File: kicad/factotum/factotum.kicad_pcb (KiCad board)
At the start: 2 copper layers, 90 x 100 mm, 146 parts, among them J1 Conn_01x06, J10 OUT3, J11 OUT5, J12 OUT7, J13 Conn_01x10_Female, J14 OUT2, J15 OUT4, J16 OUT6, J17 OUT8, J18 Conn_01x10_Male, J19 Conn_01x18_Female, J2 USART, J20 Conn_01x18_Male, J3 Conn_02x05_Odd_Even, J4 Conn_01x10_Female, J5 VOCT, J6 Conn_01x10_Male, J7 SCL, J8 CLK, J9 OUT1, P1 10k, P2 10k, P3 10k, P4 10k, SW1 MODE_SW, U1 STM32F411RETx, U10 DAC128S085, U15 PCA9685PW, U2 R-78E3.3-0.5, U3 LD2981ABU33, U4 MCP6004, U5 ADC128S022, U6 LM2902, U7 LM2902, Y1 16 MHz

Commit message: small move
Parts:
- moved D10 0.63 mm to (125.7, 41.3)
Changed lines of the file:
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@@
   )
   (module LED_THT:LED_D3.0mm-3 (layer F.Cu)
-    (at 125.73 40.64 180)
+    (at 125.73 41.275 180)
     (descr "LED, diameter 3.0mm, 2 pins, diameter 3.0mm, 3 pins, http://www.kingbright.com/attachments/file/psearch/000/00/00/L-3VSURKCGKC(Ver.8A).pdf")
     (tags "LED diameter 3.0mm 2 pins diameter 3.0mm 3 pins")

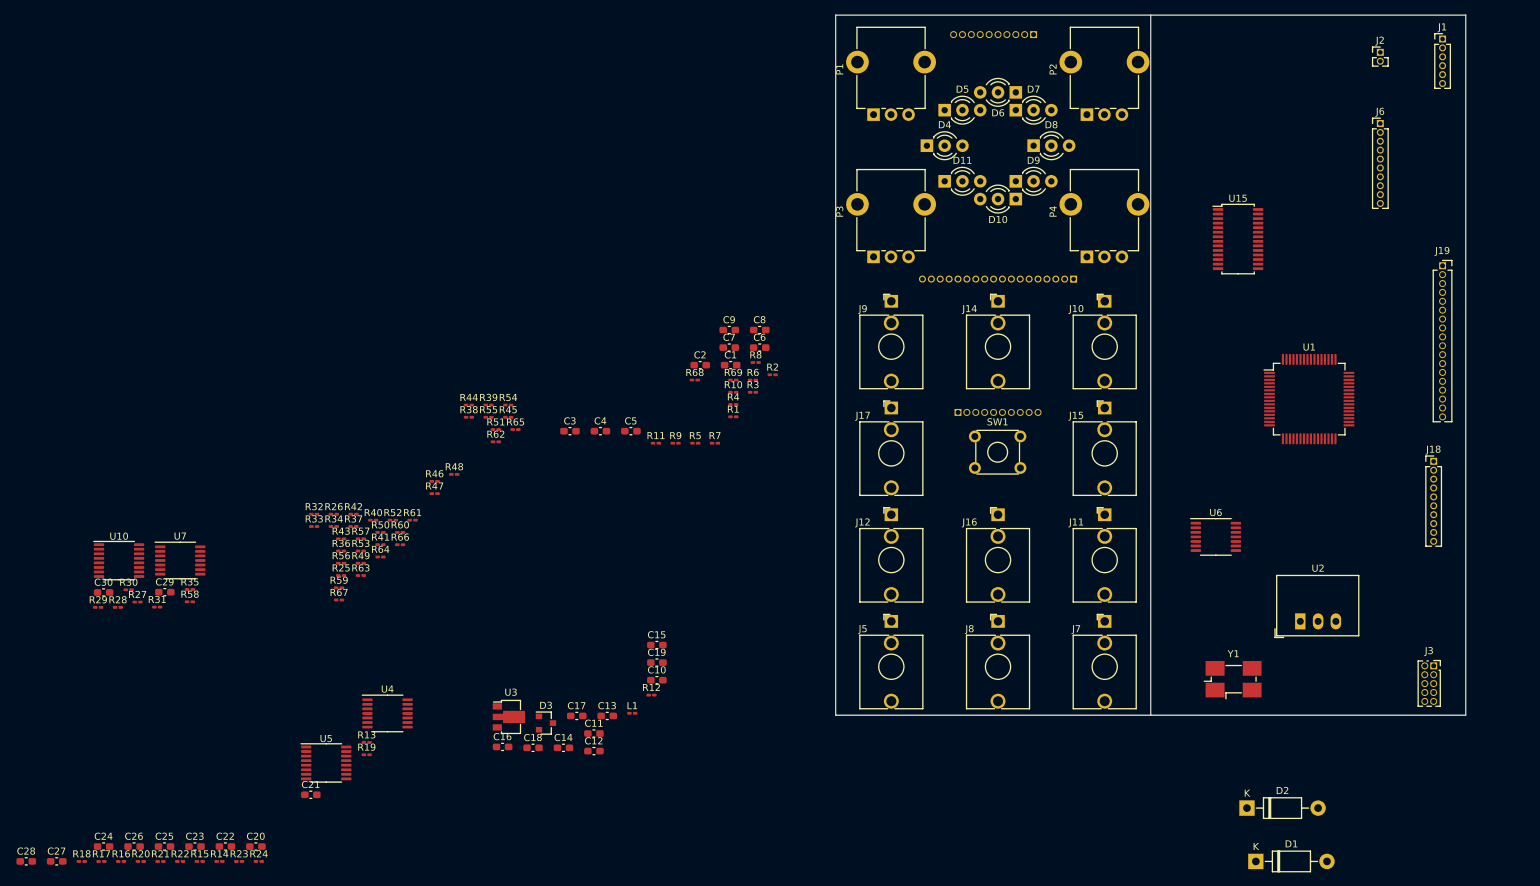
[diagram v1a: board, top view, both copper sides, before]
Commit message: inital board layout done but not routed
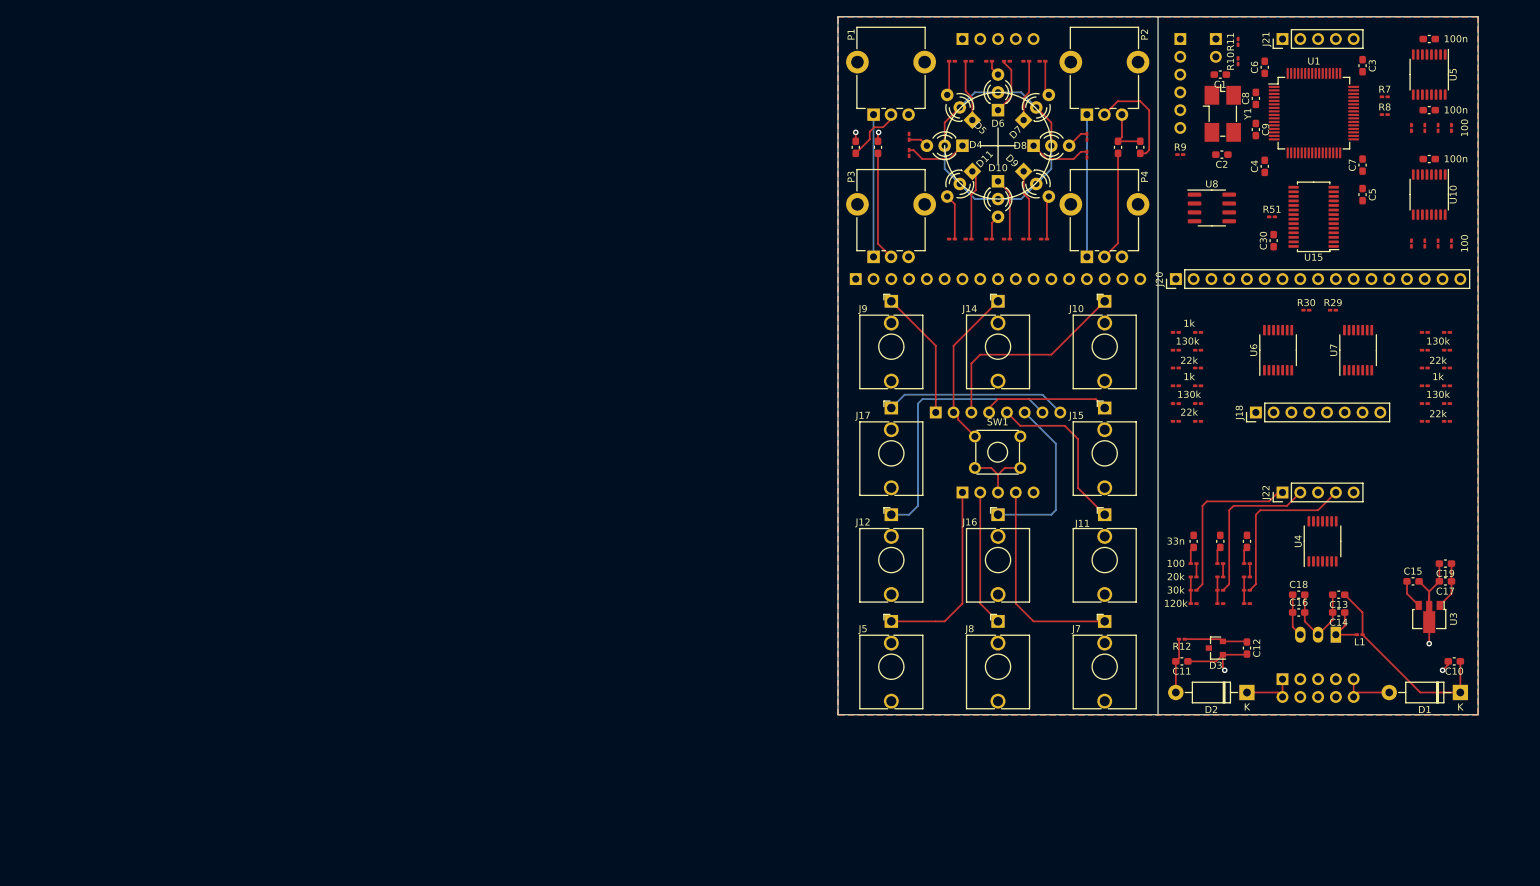
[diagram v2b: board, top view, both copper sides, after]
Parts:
- added J21: Conn_01x05_Male, Connector_PinHeader_2.54mm:PinHeader_1x05_P2.54mm_Vertical, F.Cu at (163.8, 18.4)
- added J22: Conn_01x05_Male, Connector_PinHeader_2.54mm:PinHeader_1x05_P2.54mm_Vertical, F.Cu at (163.8, 83.2)
- added U8: M24C02-RMN, Package_SO:SOIC-8_3.9x4.9mm_P1.27mm, F.Cu at (153.7, 42.5)
- J1: footprint Connector_PinHeader_1.27mm:PinHeader_1x06_P1.27mm_Vertical -> Connector_PinHeader_2.54mm:PinHeader_1x06_P2.54mm_Vertical; moved to B.Cu
- J13: value Conn_01x10_Female -> Conn_01x08_Female; footprint Connector_PinSocket_1.27mm:PinSocket_1x10_P1.27mm_Vertical -> Connector_PinSocket_2.54mm:PinSocket_1x08_P2.54mm_Vertical
- J18: value Conn_01x10_Male -> Conn_01x08_Male; footprint Connector_PinHeader_1.27mm:PinHeader_1x10_P1.27mm_Vertical -> Connector_PinHeader_2.54mm:PinHeader_1x08_P2.54mm_Vertical
- J19: value Conn_01x18_Female -> Conn_01x17_Female; footprint Connector_PinSocket_1.27mm:PinSocket_1x18_P1.27mm_Vertical -> Connector_PinSocket_2.54mm:PinSocket_1x17_P2.54mm_Vertical; moved to B.Cu
- J2: footprint Connector_PinHeader_1.27mm:PinHeader_1x02_P1.27mm_Vertical -> Connector_PinHeader_2.54mm:PinHeader_1x02_P2.54mm_Vertical; moved to B.Cu
- J20: value Conn_01x18_Male -> Conn_01x17_Male; footprint Connector_PinHeader_1.27mm:PinHeader_1x18_P1.27mm_Vertical -> Connector_PinHeader_2.54mm:PinHeader_1x17_P2.54mm_Vertical; moved to F.Cu
- J3: footprint Connector_PinSocket_1.27mm:PinSocket_2x05_P1.27mm_Vertical -> Connector_PinHeader_2.54mm:PinHeader_2x05_P2.54mm_Vertical; moved to B.Cu
- J4: value Conn_01x10_Female -> Conn_01x05_Female; footprint Connector_PinSocket_1.27mm:PinSocket_1x10_P1.27mm_Vertical -> Connector_PinSocket_2.54mm:PinSocket_1x05_P2.54mm_Vertical
- J6: value Conn_01x10_Male -> Conn_01x05_Female; footprint Connector_PinHeader_1.27mm:PinHeader_1x10_P1.27mm_Vertical -> Connector_PinSocket_2.54mm:PinSocket_1x05_P2.54mm_Vertical; moved to B.Cu
- U2: moved to B.Cu
- moved C27 223.5 mm to (184.8, 28.6), turned to 180 degrees
- moved C25 205.6 mm to (184.8, 35.6), turned to 180 degrees
- moved C29 197.1 mm to (184.8, 18.4), turned to 180 degrees
- moved U10 194.3 mm to (184.8, 40.6), turned to 270 degrees
- moved U5 185.7 mm to (184.8, 23.5), turned to 270 degrees
- moved R29 181.4 mm to (171.0, 57.1)
- moved C28 180.3 mm to (158.8, 90.2), turned to 90 degrees
- moved C30 174.5 mm to (162.6, 47.2), turned to 90 degrees
- moved R30 172.9 mm to (167.2, 57.1)
- moved C26 172.4 mm to (140.3, 33.9), turned to 90 degrees
- moved U7 170.9 mm to (174.6, 62.9), turned to 90 degrees
- moved R18 167.2 mm to (154.9, 97.2)
- moved C24 165.4 mm to (154.9, 90.2), turned to 90 degrees
- moved C22 164.5 mm to (143.5, 33.9), turned to 90 degrees
- moved R17 164.0 mm to (154.9, 99.1)
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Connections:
- net ADC_VC_SCL renamed ADC_RST
- C23 pad 1: T_SCL -> T_OFF
- C26 pad 1: T_OFF -> T_SCL
- J13 pad 1: VREF -> T_1
- J13 pad 2: T_1 -> T_2
- J13 pad 3: T_2 -> T_3
- J13 pad 4: T_3 -> T_4
- J13 pad 5: T_4 -> T_5
- J13 pad 6: T_5 -> T_6
- J13 pad 7: T_6 -> T_7
- J13 pad 8: T_7 -> T_8
- J18 pad 1: VREF -> B_1
- J18 pad 2: B_1 -> B_2
- J18 pad 3: B_2 -> B_3
- J18 pad 4: B_3 -> B_4
- J18 pad 5: B_4 -> B_5
- J18 pad 6: B_5 -> B_6
- J18 pad 7: B_6 -> B_7
- J18 pad 8: B_7 -> B_8
- J19 pad 1: +3V3 -> G8_T
- J19 pad 10: Net-(J19-Pad10) -> R4_T
- J19 pad 11: Net-(J19-Pad11) -> G3_T
- J19 pad 12: Net-(J19-Pad12) -> R3_T
- J19 pad 13: Net-(J19-Pad13) -> G2_T
- J19 pad 14: Net-(J19-Pad14) -> R2_T
- J19 pad 15: Net-(J19-Pad15) -> G1_T
- J19 pad 16: Net-(J19-Pad16) -> R1_T
- J19 pad 17: Net-(J19-Pad17) -> +3V3
- J19 pad 2: Net-(J19-Pad2) -> R8_T
- J19 pad 3: Net-(J19-Pad3) -> G7_T
- J19 pad 4: Net-(J19-Pad4) -> R7_T
- J19 pad 5: Net-(J19-Pad5) -> G6_T
- J19 pad 6: Net-(J19-Pad6) -> R6_T
- J19 pad 7: Net-(J19-Pad7) -> G5_T
- J19 pad 8: Net-(J19-Pad8) -> R5_T
- J19 pad 9: Net-(J19-Pad9) -> G4_T
- J20 pad 1: +3V3 -> Net-(J20-Pad1)
- J20 pad 10: R5_T -> Net-(J20-Pad10)
- J20 pad 11: G5_T -> Net-(J20-Pad11)
- J20 pad 12: R6_T -> Net-(J20-Pad12)
- J20 pad 13: G6_T -> Net-(J20-Pad13)
- J20 pad 14: R7_T -> Net-(J20-Pad14)
- J20 pad 15: G7_T -> Net-(J20-Pad15)
- J20 pad 16: R8_T -> Net-(J20-Pad16)
- J20 pad 17: G8_T -> +3V3
- J20 pad 2: R1_T -> Net-(J20-Pad2)
- J20 pad 3: G1_T -> Net-(J20-Pad3)
- J20 pad 4: R2_T -> Net-(J20-Pad4)
- J20 pad 5: G2_T -> Net-(J20-Pad5)
- J20 pad 6: R3_T -> Net-(J20-Pad6)
- J20 pad 7: G3_T -> Net-(J20-Pad7)
- J20 pad 8: R4_T -> Net-(J20-Pad8)
- J20 pad 9: G4_T -> Net-(J20-Pad9)
- J4 pad 3: T_SEL -> T_OFF
- J4 pad 5: T_OFF -> T_SEL
- J6 pad 1: +3.3VA -> T_VOCT
- J6 pad 2: B_FRQ -> T_CLK
- J6 pad 3: B_SEL -> T_MODE
- J6 pad 4: B_SCL -> T_RST
- J6 pad 5: B_OFF -> GND
- J7 pad S: T_SCALE -> T_RST
- P3 pad 2: T_SCL -> T_OFF
- P4 pad 2: T_OFF -> T_SCL
- R18 pad 2: B_SCALE -> B_RST
- U15 pad 10: Net-(J19-Pad6) -> Net-(J20-Pad12)
- U15 pad 11: Net-(J19-Pad7) -> Net-(J20-Pad11)
- U15 pad 12: Net-(J19-Pad8) -> Net-(J20-Pad10)
- U15 pad 13: Net-(J19-Pad9) -> Net-(J20-Pad9)
- U15 pad 15: Net-(J19-Pad10) -> Net-(J20-Pad8)
- U15 pad 16: Net-(J19-Pad11) -> Net-(J20-Pad7)
- U15 pad 17: Net-(J19-Pad12) -> Net-(J20-Pad6)
- U15 pad 18: Net-(J19-Pad13) -> Net-(J20-Pad5)
- U15 pad 19: Net-(J19-Pad14) -> Net-(J20-Pad4)
- U15 pad 20: Net-(J19-Pad15) -> Net-(J20-Pad3)
- U15 pad 21: Net-(J19-Pad16) -> Net-(J20-Pad2)
- U15 pad 22: Net-(J19-Pad17) -> Net-(J20-Pad1)
- U15 pad 6: Net-(J19-Pad2) -> Net-(J20-Pad16)
- U15 pad 7: Net-(J19-Pad3) -> Net-(J20-Pad15)
- U15 pad 8: Net-(J19-Pad4) -> Net-(J20-Pad14)
- U15 pad 9: Net-(J19-Pad5) -> Net-(J20-Pad13)
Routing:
- net +3V3: track 0.00 -> 57.0 mm
- net GND: track 0.00 -> 55.8 mm, vias 0 -> 5
- net +3.3VA: track 0.00 -> 47.3 mm
- net T_7: track 0.00 -> 37.8 mm
- net +12V: track 0.00 -> 32.7 mm
- net T_3: track 0.00 -> 29.7 mm
- net T_RST: track 0.00 -> 29.6 mm
- net T_VOCT: track 0.00 -> 27.1 mm
- net T_8: track 0.00 -> 26.0 mm
- net B_VOCT: track 0.00 -> 24.6 mm
- net T_6: track 0.00 -> 24.3 mm
- net T_5: track 0.00 -> 24.1 mm
- net B_CLK: track 0.00 -> 23.9 mm
- net B_RST: track 0.00 -> 23.0 mm
- net T_CLK: track 0.00 -> 19.5 mm
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- added copper zone on B.Cu, net GND
- added copper zone on F.Cu, net GND
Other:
- board size 90 x 100 mm -> 91.4 x 99.7 mm

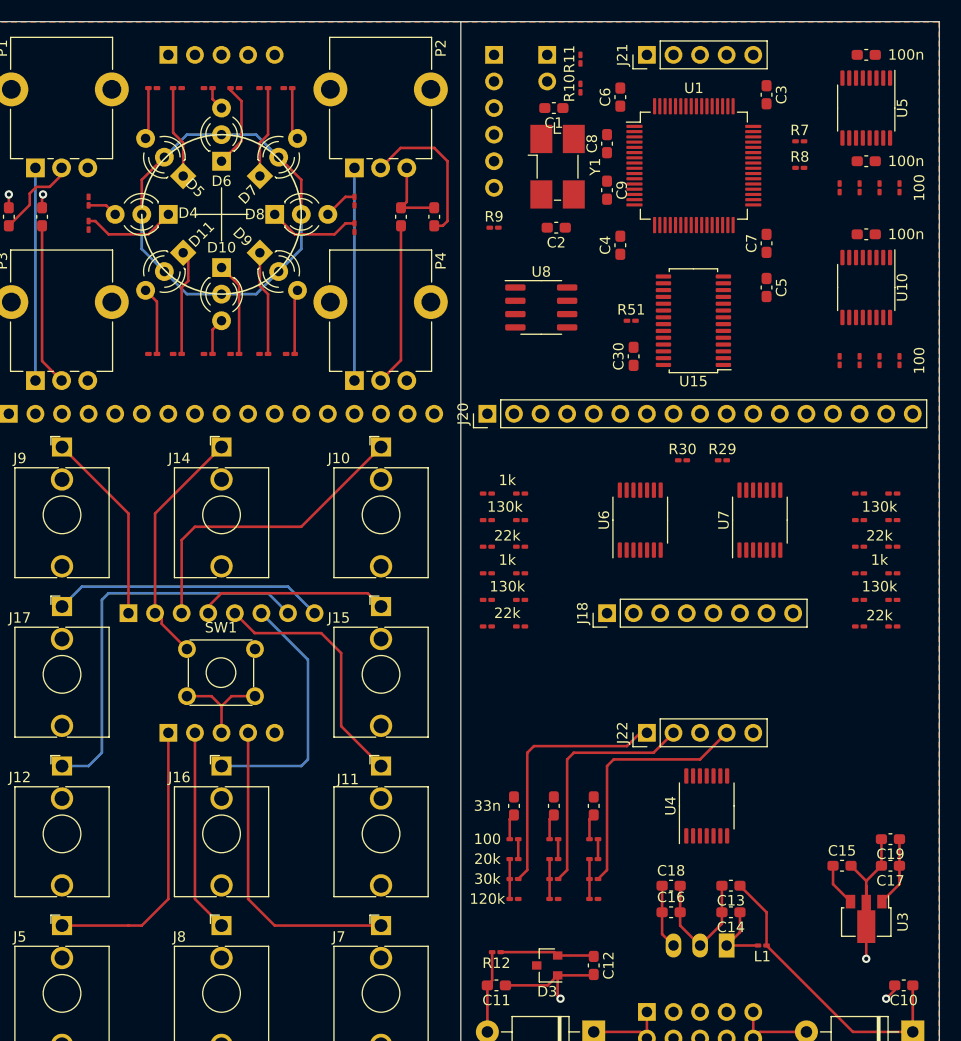
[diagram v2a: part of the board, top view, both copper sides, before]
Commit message: adding switches to inputs; fixing resistor components to 603
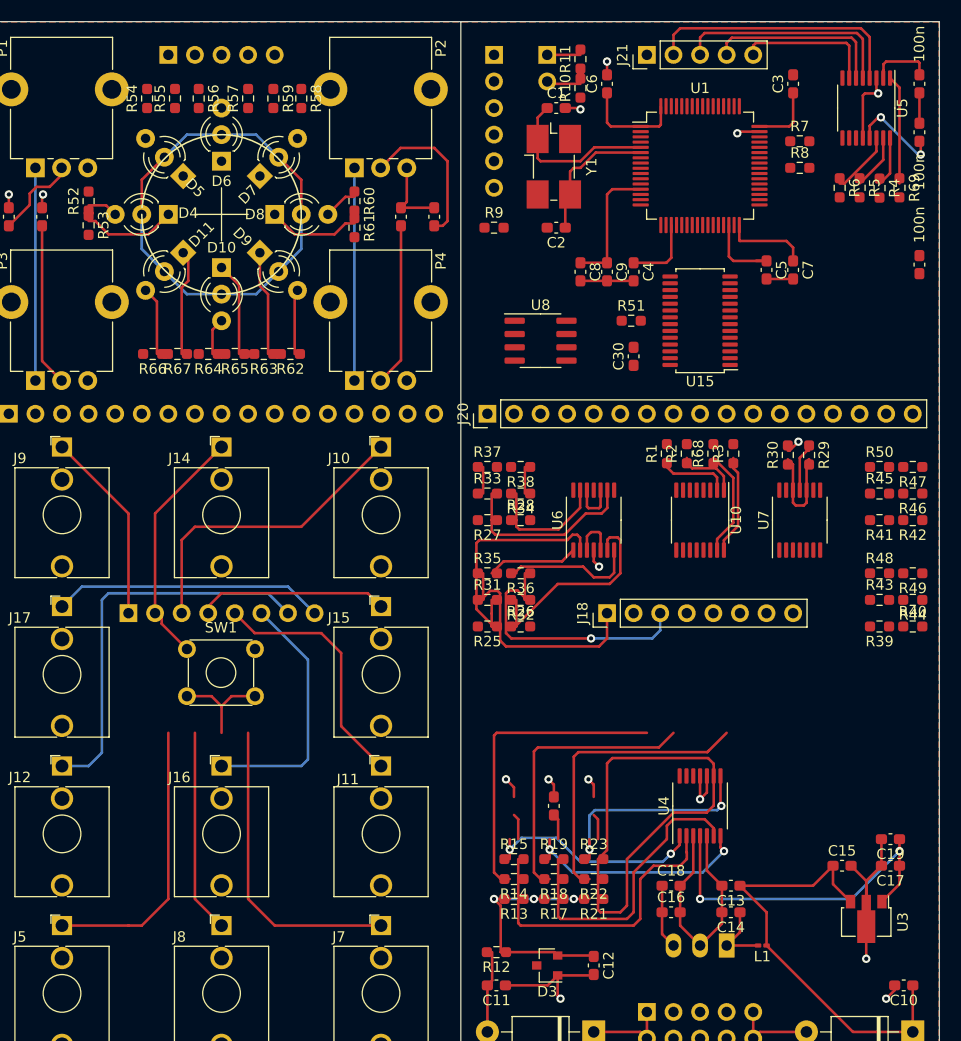
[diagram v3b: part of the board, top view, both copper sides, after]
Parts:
- removed C21, C28: 33n, Capacitor_SMD:C_0603_1608Metric_Pad1.08x0.95mm_HandSolder
- removed J22: Conn_01x05_Male, Connector_PinHeader_2.54mm:PinHeader_1x05_P2.54mm_Vertical
- removed J6: Conn_01x05_Female, Connector_PinSocket_2.54mm:PinSocket_1x05_P2.54mm_Vertical
- removed R16, R20, R24: 100, Resistor_SMD:R_0201_0603Metric_Pad0.64x0.40mm_HandSolder
- C24: value 33n -> 100p
- J7: value SCL -> RST
- R1, R10, R11, R12, R13, R15, R17, R19, R2, R21, R23, R25, R26, R27, R28, R29, R3, R30, R31, R32, R33, R34, R35, R36, R37, R38, R39, R4, R40, R41, R42, R43, R44, R45, R46, R47, R48, R49, R5, R50, R51, R52, R53, R54, R55, R56, R57, R58, R59, R6, R60, R61, R62, R63, R64, R65, R66, R67, R68, R69, R7, R8, R9: footprint Resistor_SMD:R_0201_0603Metric_Pad0.64x0.40mm_HandSolder -> Resistor_SMD:R_0603_1608Metric_Pad0.98x0.95mm_HandSolder
- R14, R18, R22: value 30k -> 120k; footprint Resistor_SMD:R_0201_0603Metric_Pad0.64x0.40mm_HandSolder -> Resistor_SMD:R_0603_1608Metric_Pad0.98x0.95mm_HandSolder
- moved U10 27.3 mm to (168.9, 62.9)
- moved R2 20.4 mm to (167.6, 56.5)
- moved R1 20.4 mm to (165.7, 56.5)
- moved R68 19.9 mm to (170.2, 56.5)
- moved R3 13.5 mm to (172.1, 56.5)
- moved C8 12.5 mm to (157.5, 39.1), turned to 270 degrees
- moved R30 10.1 mm to (177.3, 56.6), turned to 90 degrees
- moved R29 8.30 mm to (179.3, 56.6), turned to 270 degrees
- moved C9 7.80 mm to (160.0, 39.1)
- moved C25 5.85 mm to (189.9, 38.5), turned to 270 degrees
- moved C29 5.78 mm to (189.9, 21.2), turned to 270 degrees
- moved C27 5.78 mm to (189.9, 25.8), turned to 90 degrees
- moved U6 4.44 mm to (158.8, 62.9)
- moved R4 3.81 mm to (186.1, 31.1)
- moved R6 3.81 mm to (182.2, 31.1), turned to 270 degrees
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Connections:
- net Net-(U1-Pad14) renamed B_MODE_SW
- net Net-(U1-Pad15) renamed B_VOCT_SW
- net Net-(U1-Pad16) renamed B_CLK_SW
- net Net-(U1-Pad17) renamed B_RST_SW
- net T_MODE renamed T_MODE_SW
- C24 pad 1: ADC_RST -> Net-(C24-Pad1)
- C24 pad 2: GND -> ADC_VOCT
- J5 pad S: T_VOCT -> GND
- J5 pad T: GND -> T_VOCT
- J5 pad TN: GND -> T_VOCT_SW
- J7 pad S: T_RST -> GND
- J7 pad T: GND -> T_RST
- J7 pad TN: GND -> T_RST_SW
- J8 pad S: T_CLK -> GND
- J8 pad T: GND -> T_CLK
- J8 pad TN: GND -> T_CLK_SW
- R13 pad 1: Net-(R13-Pad1) -> Net-(C24-Pad1)
- R14 pad 1: Net-(R13-Pad1) -> Net-(C24-Pad1)
- R15 pad 1: Net-(R15-Pad1) -> ADC_VOCT
- R15 pad 2: Net-(R13-Pad1) -> Net-(C24-Pad1)
- R19 pad 1: Net-(R19-Pad1) -> ADC_RST
- R23 pad 1: Net-(R23-Pad1) -> ADC_CLK
- U1 pad 26: B_MODE -> Net-(U1-Pad26)
- U4 pad 1: Net-(R15-Pad1) -> ADC_VOCT
- U4 pad 2: Net-(R13-Pad1) -> Net-(C24-Pad1)
- U4 pad 7: Net-(R19-Pad1) -> ADC_RST
- U4 pad 8: Net-(R23-Pad1) -> ADC_CLK
- U5 pad 5: B_SEL -> B_OFF
- U5 pad 7: B_OFF -> B_SEL
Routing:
- net GND: track 55.8 -> 177.0 mm, vias 5 -> 14
- net +3.3VA: track 47.3 -> 97.1 mm, vias 0 -> 2
- net Net-(C28-Pad1): track 3.81 -> 47.0 mm
- net +3V3: track 57.0 -> 97.4 mm, vias 0 -> 2
- net Net-(C24-Pad1): track 0.00 -> 31.9 mm
- net T_RST: track 29.6 -> 0.00 mm
- net T_VOCT: track 27.1 -> 0.00 mm
- net B_3: track 0.00 -> 25.7 mm, vias 0 -> 1
- net B_FRQ: track 0.00 -> 25.2 mm
- net Net-(C21-Pad1): track 3.81 -> 28.5 mm
- net ADC_VOCT: track 2.48 -> 25.5 mm, vias 0 -> 3
- net Net-(R25-Pad1): track 0.00 -> 22.6 mm
- net B_1: track 0.00 -> 22.4 mm
- net B_OFF: track 0.00 -> 21.4 mm
- net ADC_CLK: track 2.48 -> 23.4 mm, vias 0 -> 2
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
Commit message: layout components again
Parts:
- added C21: 100p, Capacitor_SMD:C_0603_1608Metric_Pad1.08x0.95mm_HandSolder, F.Cu at (154.5, 84.5)
- added C28: 100p, Capacitor_SMD:C_0603_1608Metric_Pad1.08x0.95mm_HandSolder, F.Cu at (183.1, 84.5)
- added C31: 100n, Capacitor_SMD:C_0603_1608Metric_Pad1.08x0.95mm_HandSolder, F.Cu at (154.5, 99.7)
- added C32: 100n, Capacitor_SMD:C_0603_1608Metric_Pad1.08x0.95mm_HandSolder, F.Cu at (154.5, 57.8)
- added C33: 100n, Capacitor_SMD:C_0603_1608Metric_Pad1.08x0.95mm_HandSolder, F.Cu at (183.1, 57.8)
- added D12: BAT54S, Package_TO_SOT_SMD:SOT-23, F.Cu at (115.6, 110.5)
- added D13: BAT54S, Package_TO_SOT_SMD:SOT-23, F.Cu at (130.8, 110.5)
- added D14: BAT54S, Package_TO_SOT_SMD:SOT-23, F.Cu at (130.8, 95.9)
- added J22: Conn_01x08_Male, Connector_PinHeader_2.54mm:PinHeader_1x08_P2.54mm_Vertical, F.Cu at (160.0, 82.5)
- added J6: Conn_01x08_Female, Connector_PinSocket_2.54mm:PinSocket_1x08_P2.54mm_Vertical, B.Cu at (114.3, 82.5)
- added R70: 10k, Resistor_SMD:R_0603_1608Metric_Pad0.98x0.95mm_HandSolder, F.Cu at (115.6, 105.4)
- added R71: 10k, Resistor_SMD:R_0603_1608Metric_Pad0.98x0.95mm_HandSolder, F.Cu at (130.8, 77.2)
- added R72: 10k, Resistor_SMD:R_0603_1608Metric_Pad0.98x0.95mm_HandSolder, F.Cu at (130.8, 105.4)
- added R73: 10k, Resistor_SMD:R_0603_1608Metric_Pad0.98x0.95mm_HandSolder, F.Cu at (130.8, 90.8)
- L1: footprint Inductor_SMD:L_0201_0603Metric_Pad0.64x0.40mm_HandSolder -> Inductor_SMD:L_0603_1608Metric_Pad1.05x0.95mm_HandSolder
- moved C29 78.8 mm to (183.3, 99.7), turned to 0 degrees
- moved U10 30.3 mm to (174.3, 92.7), turned to 90 degrees
- moved R23 25.4 mm to (183.2, 88.3)
- moved R22 25.0 mm to (183.2, 92.1)
- moved R3 24.9 mm to (183.2, 34.3), turned to 180 degrees
- moved R21 24.7 mm to (183.2, 95.9)
- moved R2 24.1 mm to (183.2, 38.1), turned to 180 degrees
- moved R30 23.3 mm to (165.7, 76.8), turned to 180 degrees
- moved R1 22.8 mm to (183.2, 41.9), turned to 180 degrees
- moved R29 21.5 mm to (171.8, 76.8), turned to 0 degrees
- moved R9 19.0 mm to (159.7, 19.1)
- moved C4 17.0 mm to (178.2, 45.7), turned to 0 degrees
- moved R68 16.9 mm to (183.2, 45.7), turned to 180 degrees
- moved J1 16.5 mm to (148.6, 34.9)
- moved R69 14.6 mm to (188.3, 45.7), turned to 180 degrees
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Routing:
- net GND: track 177.0 -> 86.9 mm, vias 14 -> 3
- net +3.3VA: track 97.1 -> 20.3 mm, vias 2 -> 0
- net Net-(C28-Pad1): track 47.0 -> 0.00 mm
- net +3V3: track 97.4 -> 54.6 mm, vias 2 -> 0
- net +12V: track 42.4 -> 0.00 mm
- net Net-(C24-Pad1): track 31.9 -> 0.00 mm
- net B_VOCT: track 29.6 -> 0.00 mm
- net Net-(C21-Pad1): track 28.5 -> 0.00 mm
- net B_CLK: track 28.4 -> 0.00 mm
- net B_RST: track 27.4 -> 0.00 mm
- net -10V: track 26.5 -> 0.00 mm, vias 3 -> 0
- net B_3: track 25.7 -> 0.00 mm, vias 1 -> 0
- net ADC_VOCT: track 25.5 -> 0.00 mm, vias 3 -> 0
- net B_FRQ: track 25.2 -> 0.00 mm
- net ADC_CLK: track 23.4 -> 0.00 mm, vias 2 -> 0
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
